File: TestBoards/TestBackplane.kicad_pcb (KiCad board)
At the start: 18 copper layers, 70.6 x 95.5 mm, 12 parts, among them J1 BackplaneConn, J2 BackplaneConn, J3 BackplaneConn, J4 BackplaneConn, J5 BackplaneConn, J6 BackplaneConn, J7 BackplaneConn, J8 BackplaneConn

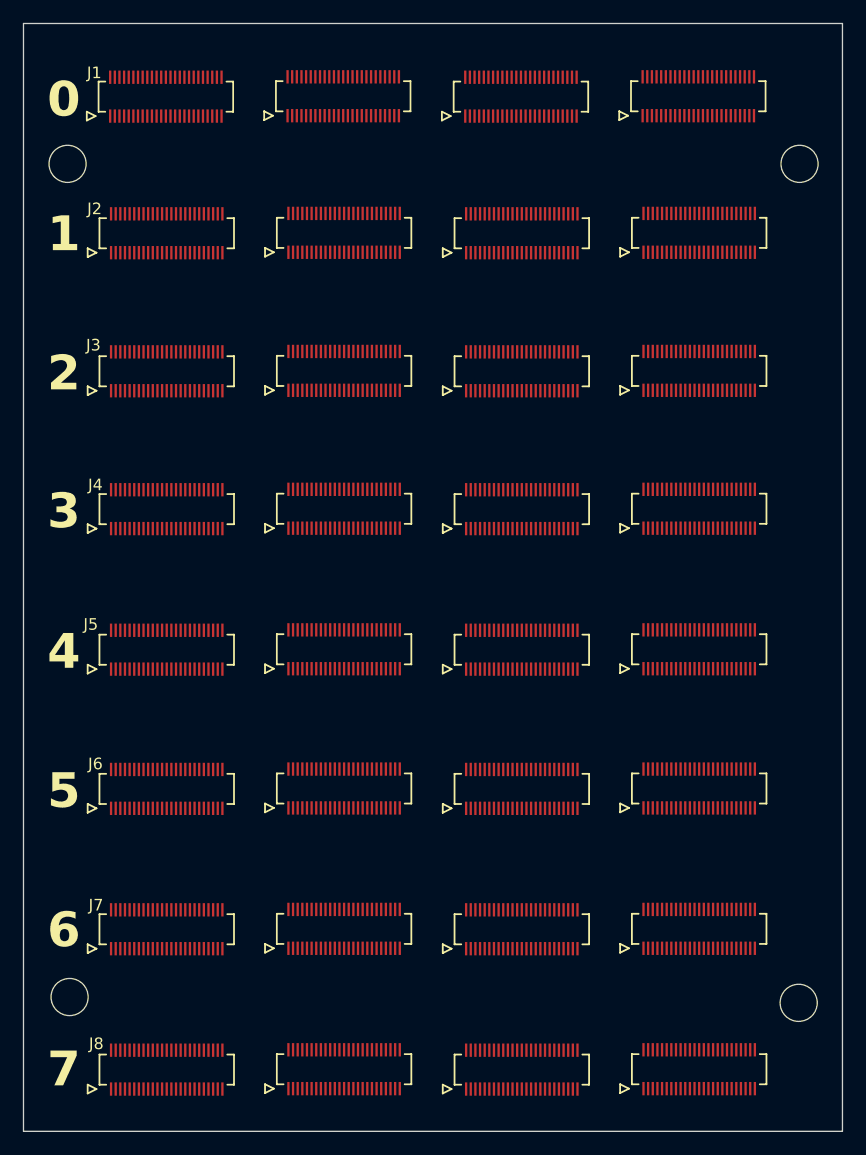
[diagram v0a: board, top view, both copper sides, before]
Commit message: test: update TestBackplane with results from successful GPU routing run (512/512 nets, 65 iters, 717s)
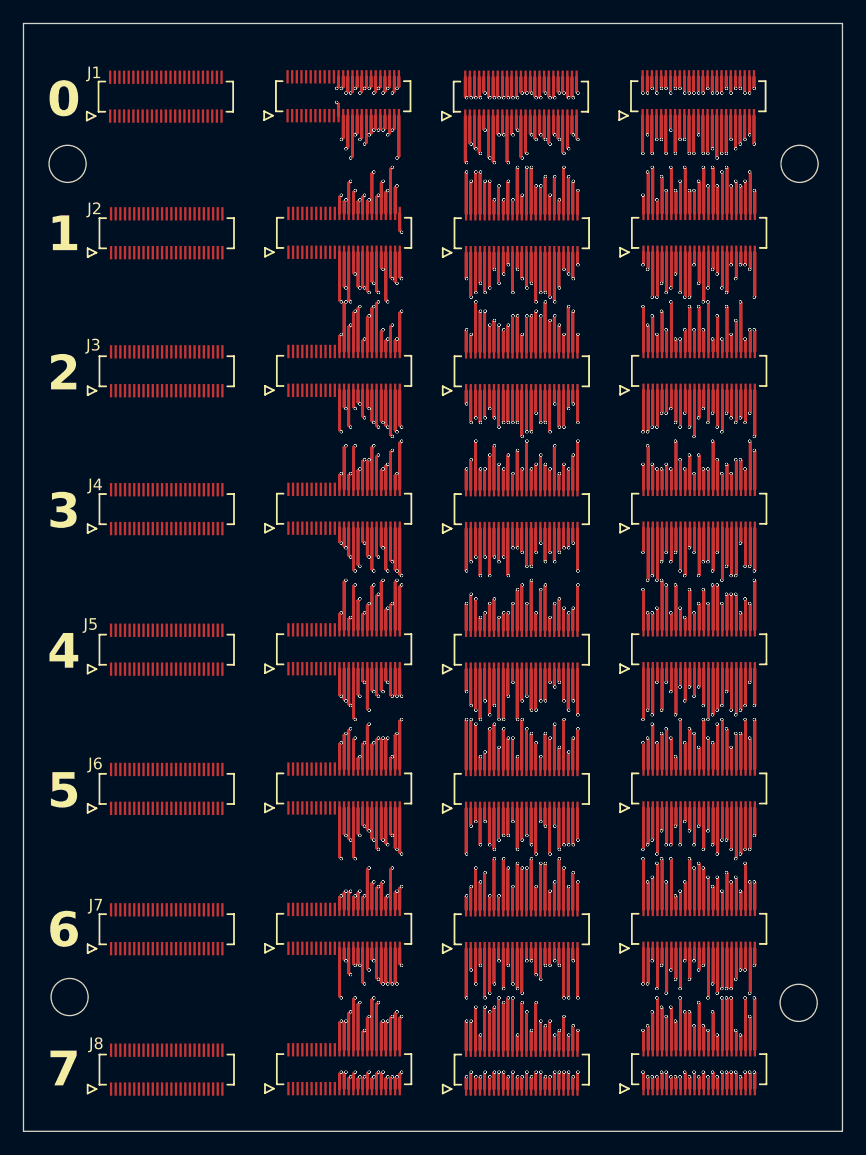
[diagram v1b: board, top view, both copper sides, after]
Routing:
- net B06B07_005: track 40.8 -> 352.1 mm, vias 2 -> 16
- net B00B04_009: track 76.8 -> 333.6 mm, vias 2 -> 29
- net B00B04_006: track 88.4 -> 302.6 mm, vias 1 -> 21
- net B08B12_001: track 49.2 -> 260.9 mm, vias 1 -> 16
- net B02B06_012: track 53.6 -> 253.5 mm, vias 1 -> 12
- net B08B10_009: track 43.6 -> 242.5 mm, vias 2 -> 14
- net B10B14_014: track 39.6 -> 234.9 mm, vias 1 -> 20
- net B01B05_004: track 4.80 -> 200.0 mm, vias 1 -> 20
- net B08B12_015: track 66.4 -> 257.9 mm, vias 1 -> 14
- net B10B14_009: track 60.8 -> 251.8 mm, vias 1 -> 28
- net B08B12_008: track 9.20 -> 199.6 mm, vias 1 -> 20
- net B08B12_000: track 0.40 -> 190.3 mm, vias 1 -> 13
- net B10B14_005: track 9.60 -> 199.0 mm, vias 1 -> 24
- net B01B05_011: track 108.4 -> 290.8 mm, vias 1 -> 13
- net B09B13_005: track 46.4 -> 227.8 mm, vias 1 -> 18
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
